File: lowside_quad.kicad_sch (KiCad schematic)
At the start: 18 parts, among them U14 2k7, U15 2k7, U28 2k7, U29 2k7, U30 RED, U31 RED, U32 RED, U33 RED, U39 MBR2H200SFT, U40 MBR2H200SFT, U45 MBR2H200SFT, U46 MBR2H200SFT, U47 NCV8403ASTT, U48 NCV8403ASTT, U49 NCV8403ASTT, U50 NCV8403ASTT

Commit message: update
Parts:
- renumbered U14 to R38, U15 to R39, U28 to R40, U29 to R41
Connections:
- net +12V renamed 12V_LED

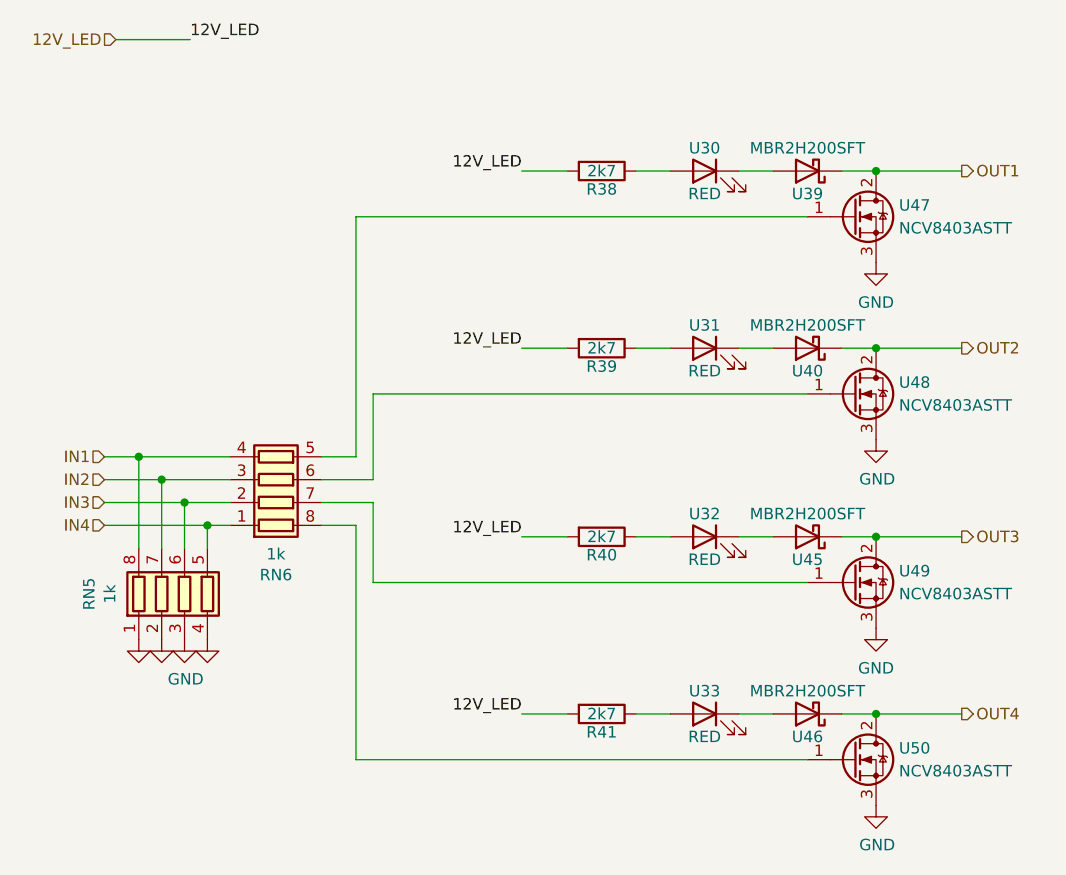
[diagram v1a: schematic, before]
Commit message: USB jack, parts and LCSC numbers, headphone jack
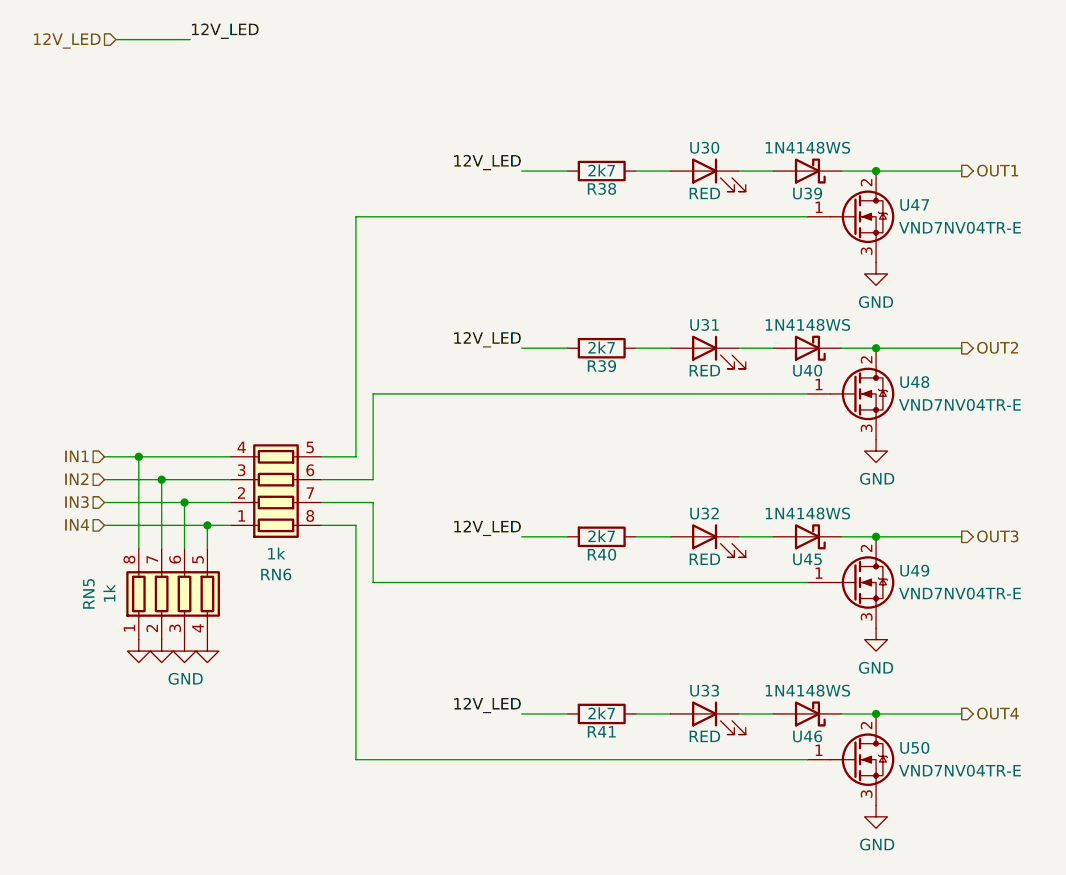
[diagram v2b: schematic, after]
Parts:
- R38, R39, R40, R41: footprint Resistor_SMD:R_0805_2012Metric -> Resistor_SMD:R_0402_1005Metric; LCSC (none) -> C138017
- U30, U31, U32, U33: footprint LED_SMD:LED_0805_2012Metric -> LED_SMD:LED_0603_1608Metric; LCSC (none) -> C84263
- U39, U40, U45, U46: value MBR2H200SFT -> 1N4148WS; footprint Diode_SMD:D_SOD-123 -> Diode_SMD:D_SOD-323; LCSC (none) -> C60580
- U47, U48, U49, U50: value NCV8403ASTT -> VND7NV04TR-E; LCSC (none) -> C155605
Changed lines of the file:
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@@
       (effects (font (size 1.27 1.27)))
     )
-    (property "Footprint" "LED_SMD:LED_0805_2012Metric" (at 125.73 56.515 0)
+    (property "Footprint" "LED_SMD:LED_0603_1608Metric" (at 125.73 56.515 0)
       (effects (font (size 1.27 1.27)) hide)
     )
@@
       (effects (font (size 1.27 1.27)))
     )
+    (property "LCSC" "C84263" (at 125.73 56.515 0)
+      (effects (font (size 1.27 1.27)) hide)
+    )
     (pin "1")
     (pin "2")
@@
       (effects (font (size 1.27 1.27)) (justify left))
     )
-    (property "Value" "NCV8403ASTT" (at 147.32 103.505 0)
+    (property "Value" "VND7NV04TR-E" (at 147.32 103.505 0)
       (effects (font (size 1.27 1.27)) (justify left))
     )
@@
       (effects (font (size 1.27 1.27)) hide)
     )
+    (property "LCSC" "C155605" (at 142.24 102.235 0)
+      (effects (font (size 1.27 1.27)) hide)
+    )
     (pin "1")
     (pin "2")
@@
       (effects (font (size 1.27 1.27)))
     )
-    (property "Value" "MBR2H200SFT" (at 137.16 34.29 0)
-      (effects (font (size 1.27 1.27)))
-    )
-    (property "Footprint" "Diode_SMD:D_SOD-123" (at 137.16 36.83 0)
+    (property "Value" "1N4148WS" (at 137.16 34.29 0)
+      (effects (font (size 1.27 1.27)))
+    )
+    (property "Footprint" "Diode_SMD:D_SOD-323" (at 137.16 36.83 0)
       (effects (font (size 1.27 1.27)) hide)
     )
@@
       (effects (font (size 1.27 1.27)))
     )
+    (property "LCSC" "C60580" (at 137.16 36.83 0)
+      (effects (font (size 1.27 1.27)) hide)
+    )
     (pin "1")
     (pin "2")
@@
       (effects (font (size 1.27 1.27)) (justify left))
     )
-    (property "Value" "NCV8403ASTT" (at 147.32 43.18 0)
+    (property "Value" "VND7NV04TR-E" (at 147.32 43.18 0)
       (effects (font (size 1.27 1.27)) (justify left))
     )
@@
       (effects (font (size 1.27 1.27)) hide)
     )
+    (property "LCSC" "C155605" (at 142.24 41.91 0)
+      (effects (font (size 1.27 1.27)) hide)
+    )
     (pin "1")
     (pin "2")
@@
       (effects (font (size 1.27 1.27)))
     )
-    (property "Value" "MBR2H200SFT" (at 137.16 94.615 0)
-      (effects (font (size 1.27 1.27)))
-    )
-    (property "Footprint" "Diode_SMD:D_SOD-123" (at 137.16 97.155 0)
+    (property "Value" "1N4148WS" (at 137.16 94.615 0)
+      (effects (font (size 1.27 1.27)))
+    )
+    (property "Footprint" "Diode_SMD:D_SOD-323" (at 137.16 97.155 0)
       (effects (font (size 1.27 1.27)) hide)
     )
@@
       (effects (font (size 1.27 1.27)))
     )
+    (property "LCSC" "C60580" (at 137.16 97.155 0)
+      (effects (font (size 1.27 1.27)) hide)
+    )
     (pin "1")
     (pin "2")
@@
       (effects (font (size 1.27 1.27)))
     )
-    (property "Footprint" "Resistor_SMD:R_0805_2012Metric" (at 114.3 95.377 90)
+    (property "Footprint" "Resistor_SMD:R_0402_1005Metric" (at 114.3 95.377 90)
       (effects (font (size 1.27 1.27)) hide)
     )
@@
       (effects (font (size 1.27 1.27)))
     )
+    (property "LCSC" "C138017" (at 114.3 97.155 90)
+      (effects (font (size 1.27 1.27)) hide)
+    )
     (pin "1")
     (pin "2")
@@
       (effects (font (size 1.27 1.27)))
     )
-    (property "Footprint" "Resistor_SMD:R_0805_2012Metric" (at 114.3 75.692 90)
+    (property "Footprint" "Resistor_SMD:R_0402_1005Metric" (at 114.3 75.692 90)
       (effects (font (size 1.27 1.27)) hide)
     )
@@
       (effects (font (size 1.27 1.27)))
     )
+    (property "LCSC" "C138017" (at 114.3 77.47 90)
+      (effects (font (size 1.27 1.27)) hide)
+    )
     (pin "1")
     (pin "2")
@@
       (effects (font (size 1.27 1.27)) (justify left))
     )
-    (property "Value" "NCV8403ASTT" (at 147.32 83.82 0)
+    (property "Value" "VND7NV04TR-E" (at 147.32 83.82 0)
       (effects (font (size 1.27 1.27)) (justify left))
     )
@@
       (effects (font (size 1.27 1.27)) hide)
     )
+    (property "LCSC" "C155605" (at 142.24 82.55 0)
+      (effects (font (size 1.27 1.27)) hide)
+    )
     (pin "1")
     (pin "2")
@@
       (effects (font (size 1.27 1.27)))
     )
-    (property "Footprint" "LED_SMD:LED_0805_2012Metric" (at 125.73 97.155 0)
+    (property "Footprint" "LED_SMD:LED_0603_1608Metric" (at 125.73 97.155 0)
       (effects (font (size 1.27 1.27)) hide)
     )
@@
       (effects (font (size 1.27 1.27)))
     )
+    (property "LCSC" "C84263" (at 125.73 97.155 0)
+      (effects (font (size 1.27 1.27)) hide)
+    )
     (pin "1")
     (pin "2")
@@
       (effects (font (size 1.27 1.27)))
     )
-    (property "Footprint" "Resistor_SMD:R_0805_2012Metric" (at 114.3 35.052 90)
+    (property "Footprint" "Resistor_SMD:R_0402_1005Metric" (at 114.3 35.052 90)
       (effects (font (size 1.27 1.27)) hide)
     )
@@
       (effects (font (size 1.27 1.27)))
     )
+    (property "LCSC" "C138017" (at 114.3 36.83 90)
+      (effects (font (size 1.27 1.27)) hide)
+    )
     (pin "1")
     (pin "2")
@@
       (effects (font (size 1.27 1.27)))
     )
-    (property "Footprint" "Resistor_SMD:R_0805_2012Metric" (at 114.3 54.737 90)
+    (property "Footprint" "Resistor_SMD:R_0402_1005Metric" (at 114.3 54.737 90)
       (effects (font (size 1.27 1.27)) hide)
     )
@@
       (effects (font (size 1.27 1.27)))
     )
+    (property "LCSC" "C138017" (at 114.3 56.515 90)
+      (effects (font (size 1.27 1.27)) hide)
+    )
     (pin "1")
     (pin "2")
@@
       (effects (font (size 1.27 1.27)))
     )
-    (property "Value" "MBR2H200SFT" (at 137.16 53.975 0)
-      (effects (font (size 1.27 1.27)))
-    )
-    (property "Footprint" "Diode_SMD:D_SOD-123" (at 137.16 56.515 0)
+    (property "Value" "1N4148WS" (at 137.16 53.975 0)
+      (effects (font (size 1.27 1.27)))
+    )
+    (property "Footprint" "Diode_SMD:D_SOD-323" (at 137.16 56.515 0)
       (effects (font (size 1.27 1.27)) hide)
     )
@@
       (effects (font (size 1.27 1.27)))
     )
+    (property "LCSC" "C60580" (at 137.16 56.515 0)
+      (effects (font (size 1.27 1.27)) hide)
+    )
     (pin "1")
     (pin "2")
@@
       (effects (font (size 1.27 1.27)) (justify left))
     )
-    (property "Value" "NCV8403ASTT" (at 147.32 62.865 0)
+    (property "Value" "VND7NV04TR-E" (at 147.32 62.865 0)
       (effects (font (size 1.27 1.27)) (justify left))
     )
@@
       (effects (font (size 1.27 1.27)) hide)
     )
+    (property "LCSC" "C155605" (at 142.24 61.595 0)
+      (effects (font (size 1.27 1.27)) hide)
+    )
     (pin "1")
     (pin "2")
@@
       (effects (font (size 1.27 1.27)))
     )
-    (property "Footprint" "LED_SMD:LED_0805_2012Metric" (at 125.73 36.83 0)
+    (property "Footprint" "LED_SMD:LED_0603_1608Metric" (at 125.73 36.83 0)
       (effects (font (size 1.27 1.27)) hide)
     )
@@
       (effects (font (size 1.27 1.27)))
     )
+    (property "LCSC" "C84263" (at 125.73 36.83 0)
+      (effects (font (size 1.27 1.27)) hide)
+    )
     (pin "1")
     (pin "2")
@@
       (effects (font (size 1.27 1.27)))
     )
-    (property "Value" "MBR2H200SFT" (at 137.16 74.93 0)
-      (effects (font (size 1.27 1.27)))
-    )
-    (property "Footprint" "Diode_SMD:D_SOD-123" (at 137.16 77.47 0)
+    (property "Value" "1N4148WS" (at 137.16 74.93 0)
+      (effects (font (size 1.27 1.27)))
+    )
+    (property "Footprint" "Diode_SMD:D_SOD-323" (at 137.16 77.47 0)
       (effects (font (size 1.27 1.27)) hide)
     )
@@
       (effects (font (size 1.27 1.27)))
     )
+    (property "LCSC" "C60580" (at 137.16 77.47 0)
+      (effects (font (size 1.27 1.27)) hide)
+    )
     (pin "1")
     (pin "2")
@@
       (effects (font (size 1.27 1.27)))
     )
-    (property "Footprint" "LED_SMD:LED_0805_2012Metric" (at 125.73 77.47 0)
+    (property "Footprint" "LED_SMD:LED_0603_1608Metric" (at 125.73 77.47 0)
       (effects (font (size 1.27 1.27)) hide)
     )
@@
       (effects (font (size 1.27 1.27)))
     )
-    (pin "1")
+    (property "LCSC" "C84263" (at 125.73 77.47 0)
+      (effects (font (size 1.27 1.27)) hide)
+    )
+    (pin "1")

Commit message: Add Stepper, fix Connector, add Testpoints, several changes
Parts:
- U30, U31, U32, U33: LCSC C84263 -> C2286
- U39, U40, U45, U46: LCSC C60580 -> C2128
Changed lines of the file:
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@@
       (effects (font (size 1.27 1.27)))
     )
-    (property "LCSC" "C84263" (at 125.73 56.515 0)
+    (property "LCSC" "C2286" (at 125.73 56.515 0)
       (effects (font (size 1.27 1.27)) hide)
     )
@@
       (effects (font (size 1.27 1.27)))
     )
-    (property "LCSC" "C60580" (at 137.16 36.83 0)
+    (property "LCSC" "C2128" (at 137.16 36.83 0)
       (effects (font (size 1.27 1.27)) hide)
     )
@@
       (effects (font (size 1.27 1.27)))
     )
-    (property "LCSC" "C60580" (at 137.16 97.155 0)
+    (property "LCSC" "C2128" (at 137.16 97.155 0)
       (effects (font (size 1.27 1.27)) hide)
     )
@@
       (effects (font (size 1.27 1.27)))
     )
-    (property "LCSC" "C84263" (at 125.73 97.155 0)
+    (property "LCSC" "C2286" (at 125.73 97.155 0)
       (effects (font (size 1.27 1.27)) hide)
     )
@@
       (effects (font (size 1.27 1.27)))
     )
-    (property "LCSC" "C60580" (at 137.16 56.515 0)
+    (property "LCSC" "C2128" (at 137.16 56.515 0)
       (effects (font (size 1.27 1.27)) hide)
     )
@@
       (effects (font (size 1.27 1.27)))
     )
-    (property "LCSC" "C84263" (at 125.73 36.83 0)
+    (property "LCSC" "C2286" (at 125.73 36.83 0)
       (effects (font (size 1.27 1.27)) hide)
     )
@@
       (effects (font (size 1.27 1.27)))
     )
-    (property "LCSC" "C60580" (at 137.16 77.47 0)
+    (property "LCSC" "C2128" (at 137.16 77.47 0)
       (effects (font (size 1.27 1.27)) hide)
     )
@@
       (effects (font (size 1.27 1.27)))
     )
-    (property "LCSC" "C84263" (at 125.73 77.47 0)
-      (effects (font (size 1.27 1.27)) hide)
-    )
+    (property "LCSC" "C2286" (at 125.73 77.47 0)
+      (effects (font (size 1.27 1.27)) hide)
+    )
